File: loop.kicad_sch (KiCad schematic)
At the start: 0 parts

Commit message: schematic
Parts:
- added BT1: Battery_Cell, Package_DFN_QFN:QFN-40-1EP_6x6mm_P0.5mm_EP4.6x4.6mm, symbol Device:Battery_Cell
- added D1: LED, symbol Device:LED
- added SW1: SW_SPST, symbol Switch:SW_SPST
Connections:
- new net: BT1.2 (-), D1.1 (K)
- new net: D1.2 (A), SW1.2 (B)
- new net: BT1.1 (+), SW1.1 (A)

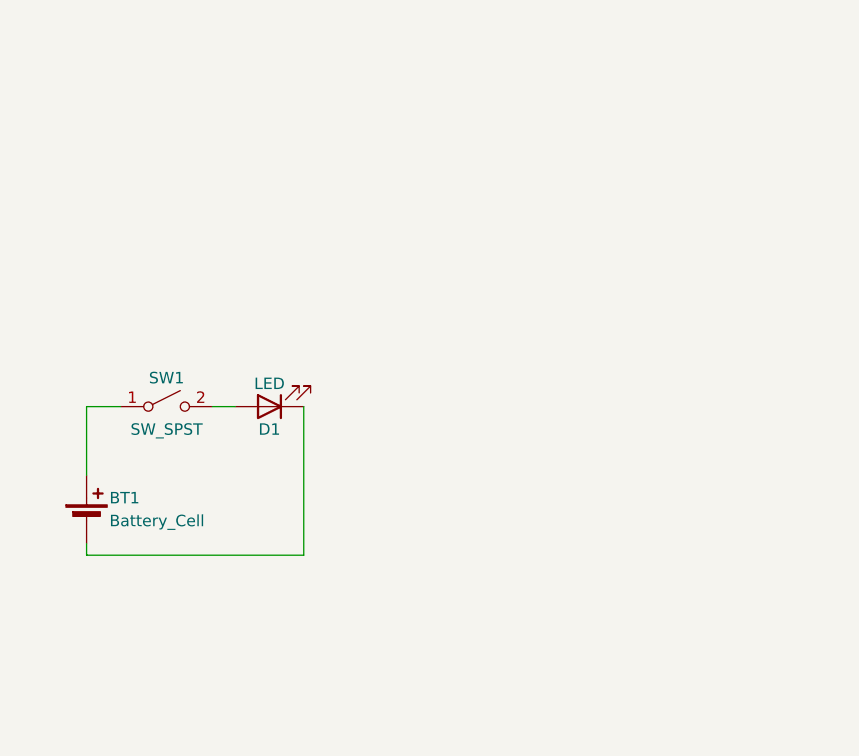
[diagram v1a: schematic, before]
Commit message: build latch schematic using dual flip flop
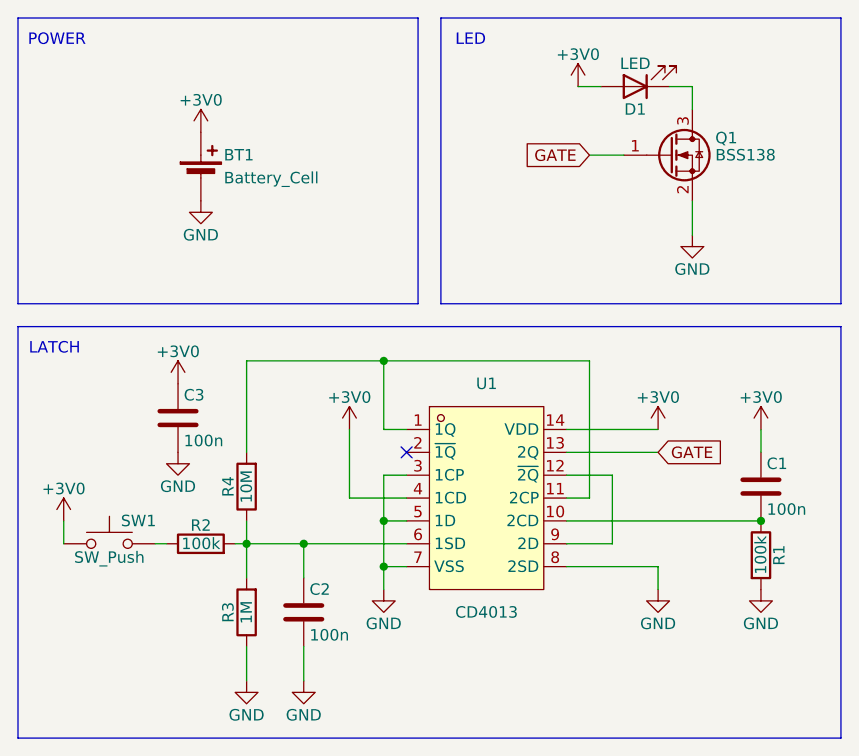
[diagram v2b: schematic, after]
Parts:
- removed SW1: SW_SPST, symbol Switch:SW_SPST
- added C1, C2, C3: 100n, Package_TO_SOT_SMD:SOT-23, symbol Device:C
- added Q1: BSS138, Package_TO_SOT_SMD:SOT-23, symbol Transistor_FET:BSS138
- added R1, R2: 100k, symbol Device:R
- added R3: 1M, symbol Device:R
- added R4: 10M, symbol Device:R
- added SW1: SW_Push, SparkFun-Switch:Push_PTH_12x12mm, symbol Switch:SW_Push
- added U1: CD4013, easyeda2kicad:SOP-14_L8.7-W3.9-P1.27-LS6.0-BL, symbol LCSC:CD4013
- BT1: footprint Package_DFN_QFN:QFN-40-1EP_6x6mm_P0.5mm_EP4.6x4.6mm -> Battery:BatteryHolder_Multicomp_BC-2001_1x2032
- D1: footprint (none) -> 0_CustomFootprints:Led Nood
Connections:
- net at D1.1 (K): now also Q1.3 (D); no longer BT1.2 (-)
- net +3V0: now reaches D1.2 (A)
- net +3V0: now also BT1.1 (+), C1.1, C3.1, SW1.1, U1.14 (VDD), U1.4 (1CD)
- new net: C2.1, R2.2, R3.2, R4.1, U1.6 (1SD)
- new net: R4.2, U1.1 (1Q), U1.11 (2CP)
- new net: C1.2, R1.1, U1.10 (2CD)
- new net: U1.12 (~{2Q}), U1.9 (2D)
- new net: R2.1, SW1.2
- new net GATE: Q1.1 (G), U1.13 (2Q)
- new net GND: BT1.2 (-), C2.2, C3.2, Q1.2 (S), R1.2, R3.1, U1.3 (1CP), U1.5 (1D), U1.7 (VSS), U1.8 (2SD)
- no-connect marks 0 -> 1
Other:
- note added: "LATCH"
- note added: "LED"
- note added: "POWER"
- company: (none) -> Paul Methfessel
- title: (none) -> Loop
- moved on the sheet: BT1, D1

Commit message: build pcb layout
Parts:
- C1, C2, C3: footprint Package_TO_SOT_SMD:SOT-23 -> Capacitor_SMD:C_0805_2012Metric_Pad1.18x1.45mm_HandSolder
- R1, R2, R3, R4: footprint (none) -> Resistor_SMD:R_0805_2012Metric_Pad1.20x1.40mm_HandSolder
- SW1: footprint SparkFun-Switch:Push_PTH_12x12mm -> Button_Switch_SMD:SW_SPST_TL3342
- U1: footprint easyeda2kicad:SOP-14_L8.7-W3.9-P1.27-LS6.0-BL -> LCSC:SOP-14_L8.7-W3.9-P1.27-LS6.0-BL
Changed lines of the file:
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@@
 			)
 		)
-		(property "Footprint" "Package_TO_SOT_SMD:SOT-23"
+		(property "Footprint" "Capacitor_SMD:C_0805_2012Metric_Pad1.18x1.45mm_HandSolder"
 			(at 116.5352 92.71 0)
 			(hide yes)
@@
 			)
 		)
-		(property "Footprint" ""
+		(property "Footprint" "Resistor_SMD:R_0805_2012Metric_Pad1.20x1.40mm_HandSolder"
 			(at 124.968 96.52 90)
 			(hide yes)
@@
 			)
 		)
-		(property "Footprint" ""
+		(property "Footprint" "Resistor_SMD:R_0805_2012Metric_Pad1.20x1.40mm_HandSolder"
 			(at 178.562 104.14 90)
 			(hide yes)
@@
 			)
 		)
-		(property "Footprint" "easyeda2kicad:SOP-14_L8.7-W3.9-P1.27-LS6.0-BL"
+		(property "Footprint" "LCSC:SOP-14_L8.7-W3.9-P1.27-LS6.0-BL"
 			(at 149.86 113.03 0)
 			(hide yes)
@@
 			)
 		)
-		(property "Footprint" "Package_TO_SOT_SMD:SOT-23"
+		(property "Footprint" "Capacitor_SMD:C_0805_2012Metric_Pad1.18x1.45mm_HandSolder"
 			(at 181.3052 100.33 0)
 			(hide yes)
@@
 			)
 		)
-		(property "Footprint" ""
+		(property "Footprint" "Resistor_SMD:R_0805_2012Metric_Pad1.20x1.40mm_HandSolder"
 			(at 124.968 110.49 90)
 			(hide yes)
@@
 			)
 		)
-		(property "Footprint" ""
+		(property "Footprint" "Resistor_SMD:R_0805_2012Metric_Pad1.20x1.40mm_HandSolder"
 			(at 118.11 104.648 90)
 			(hide yes)
@@
 			)
 		)
-		(property "Footprint" "Package_TO_SOT_SMD:SOT-23"
+		(property "Footprint" "Capacitor_SMD:C_0805_2012Metric_Pad1.18x1.45mm_HandSolder"
 			(at 130.5052 114.3 0)
 			(hide yes)
@@
 			)
 		)
-		(property "Footprint" "SparkFun-Switch:Push_PTH_12x12mm"
+		(property "Footprint" "Button_Switch_SMD:SW_SPST_TL3342"
 			(at 107.95 97.79 0)
 			(hide yes)

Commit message: Add series r
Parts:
- removed C3: 100n, Capacitor_SMD:C_0805_2012Metric_Pad1.18x1.45mm_HandSolder, symbol Device:C
- added C4: 22u, Capacitor_SMD:C_0805_2012Metric_Pad1.18x1.45mm_HandSolder, symbol Device:C
- added C5: 10u, Capacitor_SMD:C_0805_2012Metric_Pad1.18x1.45mm_HandSolder, symbol Device:C
- added R5: 1k, Resistor_SMD:R_0805_2012Metric_Pad1.20x1.40mm_HandSolder, symbol Device:R
- added R6: 33, Resistor_SMD:R_0805_2012Metric_Pad1.20x1.40mm_HandSolder, symbol Device:R
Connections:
- net +3V0: now also C4.1, R5.1, R6.1; no longer D1.2 (A), U1.14 (VDD), U1.4 (1CD)
- net GND: now also C4.2, C5.2
- new net: D1.2 (A), R6.2
- new net V_F: C5.1, R5.2, U1.14 (VDD), U1.4 (1CD)
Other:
- moved on the sheet: BT1, C1, D1, Q1, R1

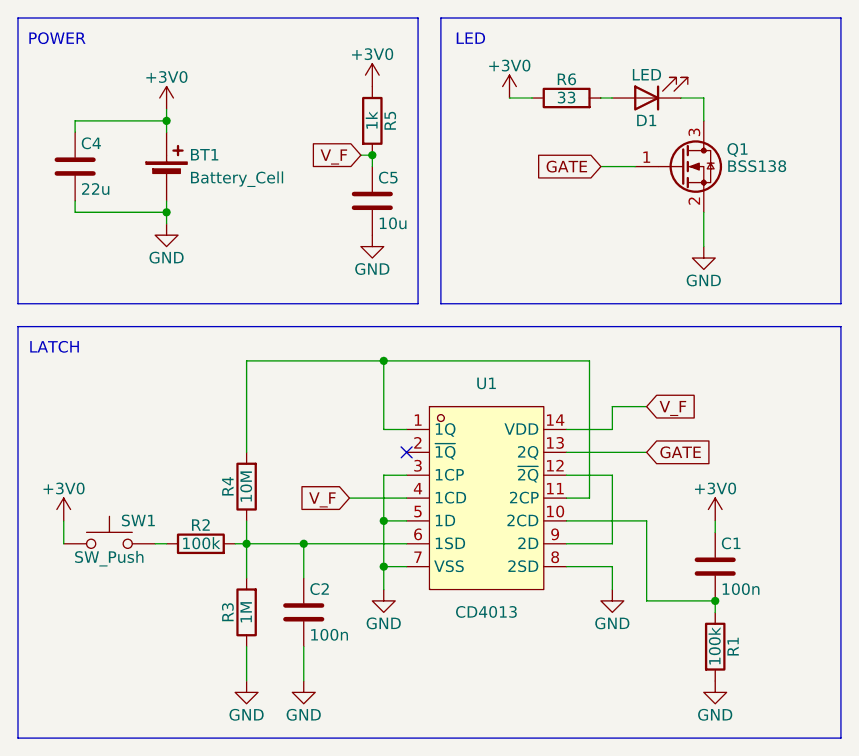
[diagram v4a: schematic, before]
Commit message: Use Attiny202
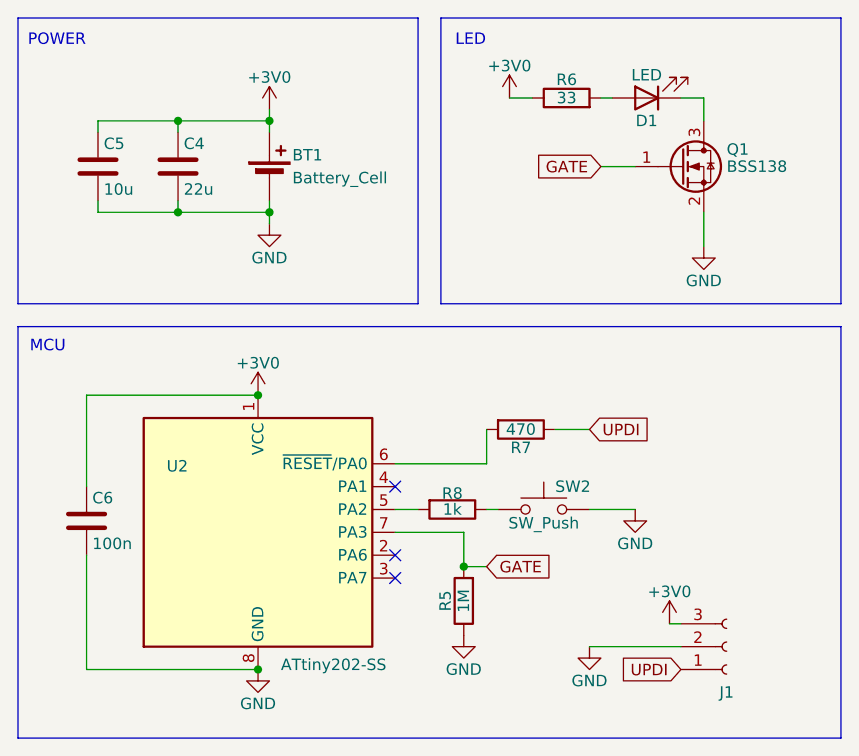
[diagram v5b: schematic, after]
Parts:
- removed C1, C2: 100n, Capacitor_SMD:C_0805_2012Metric_Pad1.18x1.45mm_HandSolder, symbol Device:C
- removed R1, R2: 100k, Resistor_SMD:R_0805_2012Metric_Pad1.20x1.40mm_HandSolder, symbol Device:R
- removed R3: 1M, Resistor_SMD:R_0805_2012Metric_Pad1.20x1.40mm_HandSolder, symbol Device:R
- removed R4: 10M, Resistor_SMD:R_0805_2012Metric_Pad1.20x1.40mm_HandSolder, symbol Device:R
- removed SW1: SW_Push, Button_Switch_SMD:SW_SPST_TL3342, symbol Switch:SW_Push
- removed U1: CD4013, LCSC:SOP-14_L8.7-W3.9-P1.27-LS6.0-BL, symbol LCSC:CD4013
- added C6: 100n, Capacitor_SMD:C_0805_2012Metric_Pad1.18x1.45mm_HandSolder, symbol Device:C
- added J1: Conn_01x03_Socket, Connector:Tag-Connect_TC2030-IDC-FP_2x03_P1.27mm_Vertical, symbol Connector:Conn_01x03_Socket
- added R7: 470, Resistor_SMD:R_0805_2012Metric_Pad1.20x1.40mm_HandSolder, symbol Device:R
- added R8: 1k, Resistor_SMD:R_0805_2012Metric_Pad1.20x1.40mm_HandSolder, symbol Device:R
- added SW2: SW_Push, Button_Switch_SMD:SW_SPST_TL3342, symbol Switch:SW_Push
- added U2: ATtiny202-SS, Package_SO:SOIC-8_3.9x4.9mm_P1.27mm, symbol MCU_Microchip_ATtiny:ATtiny202-SS
- R5: value 1k -> 1M
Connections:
- net +3V0: now also C5.1, C6.1, J1.3 (Pin_3), U2.1 (VCC); no longer R5.1
- net GATE: now also R5.2, U2.7 (PA3)
- net GND: now also R5.1, C6.2, J1.2 (Pin_2), SW2.2, U2.8 (GND)
- removed net V_F: C5.1, R5.2
- new net: R8.1, SW2.1
- new net: R8.2, U2.5 (PA2)
- new net: R7.2, U2.6 (~{RESET}/PA0)
- new net UPDI: J1.1 (Pin_1), R7.1
- no-connect marks 1 -> 3
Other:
- note added: "MCU"
- note removed: "LATCH"
- moved on the sheet: BT1, C4

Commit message: Update PCB
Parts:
- BT1: footprint Battery:BatteryHolder_Multicomp_BC-2001_1x2032 -> easyeda2kicad:BAT-SMD_MY-1220-03
- J1: footprint Connector:Tag-Connect_TC2030-IDC-FP_2x03_P1.27mm_Vertical -> Connector_PinSocket_2.54mm:PinSocket_1x03_P2.54mm_Vertical
- renumbered C6 to C1, C5 to C2, C4 to C3, R8 to R1, R5 to R2, R7 to R3, R6 to R4, SW2 to SW1, U2 to U1
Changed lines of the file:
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@@
 		(in_pos_files yes)
 		(dnp no)
-		(property "Reference" "C4"
+		(property "Reference" "C3"
 			(at 116.205 58.42 0)
 			(show_name no)
@@
 			(project "loop"
 				(path "/b044b678-0750-420d-a2ee-3e7506caa1d8"
-					(reference "C4")
+					(reference "C3")
 					(unit 1)
 				)
@@
 		(in_pos_files yes)
 		(dnp no)
-		(property "Reference" "C6"
+		(property "Reference" "C1"
 			(at 106.045 97.79 0)
 			(show_name no)
@@
 			(project "loop"
 				(path "/b044b678-0750-420d-a2ee-3e7506caa1d8"
-					(reference "C6")
+					(reference "C1")
 					(unit 1)
 				)
@@
 		(in_pos_files yes)
 		(dnp no)
-		(property "Reference" "#PWR04"
+		(property "Reference" "#PWR09"
 			(at 170.18 115.57 0)
 			(hide yes)
@@
 			(project "loop"
 				(path "/b044b678-0750-420d-a2ee-3e7506caa1d8"
-					(reference "#PWR04")
+					(reference "#PWR09")
 					(unit 1)
 				)
@@
 		(in_pos_files yes)
 		(dnp no)
-		(property "Reference" "R5"
+		(property "Reference" "R2"
 			(at 145.288 109.22 90)
 			(show_name no)
@@
 			(project "loop"
 				(path "/b044b678-0750-420d-a2ee-3e7506caa1d8"
-					(reference "R5")
+					(reference "R2")
 					(unit 1)
 				)
@@
 		(in_pos_files yes)
 		(dnp no)
-		(property "Reference" "#PWR08"
+		(property "Reference" "#PWR010"
 			(at 173.99 76.2 0)
 			(hide yes)
@@
 			(project "loop"
 				(path "/b044b678-0750-420d-a2ee-3e7506caa1d8"
-					(reference "#PWR08")
+					(reference "#PWR010")
 					(unit 1)
 				)
@@
 		(in_pos_files yes)
 		(dnp no)
-		(property "Reference" "#PWR015"
+		(property "Reference" "#PWR05"
 			(at 147.32 119.38 0)
 			(hide yes)
@@
 			(project "loop"
 				(path "/b044b678-0750-420d-a2ee-3e7506caa1d8"
-					(reference "#PWR015")
+					(reference "#PWR05")
 					(unit 1)
 				)
@@
 		(in_pos_files yes)
 		(dnp no)
-		(property "Reference" "R8"
+		(property "Reference" "R1"
 			(at 146.05 97.282 90)
 			(show_name no)
@@
 			(project "loop"
 				(path "/b044b678-0750-420d-a2ee-3e7506caa1d8"
-					(reference "R8")
+					(reference "R1")
 					(unit 1)
 				)
@@
 		(in_pos_files yes)
 		(dnp no)
-		(property "Reference" "C5"
+		(property "Reference" "C2"
 			(at 107.315 58.42 0)
 			(show_name no)
@@
 			(project "loop"
 				(path "/b044b678-0750-420d-a2ee-3e7506caa1d8"
-					(reference "C5")
+					(reference "C2")
 					(unit 1)
 				)
@@
 			)
 		)
-		(property "Footprint" "Connector:Tag-Connect_TC2030-IDC-FP_2x03_P1.27mm_Vertical"
+		(property "Footprint" "Connector_PinSocket_2.54mm:PinSocket_1x03_P2.54mm_Vertical"
 			(at 176.53 114.3 0)
 			(hide yes)
@@
 		(in_pos_files yes)
 		(dnp no)
-		(property "Reference" "SW2"
+		(property "Reference" "SW1"
 			(at 157.48 96.52 0)
 			(show_name no)
@@
 			(project "loop"
 				(path "/b044b678-0750-420d-a2ee-3e7506caa1d8"
-					(reference "SW2")
+					(reference "SW1")
 					(unit 1)
 				)
@@
 		(in_pos_files yes)
 		(dnp no)
-		(property "Reference" "#PWR017"
+		(property "Reference" "#PWR07"
 			(at 161.29 120.65 0)
 			(hide yes)
@@
 			(project "loop"
 				(path "/b044b678-0750-420d-a2ee-3e7506caa1d8"
-					(reference "#PWR017")
+					(reference "#PWR07")
 					(unit 1)
 				)
@@
 		(in_pos_files yes)
 		(dnp no)
-		(property "Reference" "#PWR07"
+		(property "Reference" "#PWR06"
 			(at 152.4 57.15 0)
 			(hide yes)
@@
 			(project "loop"
 				(path "/b044b678-0750-420d-a2ee-3e7506caa1d8"
-					(reference "#PWR07")
+					(reference "#PWR06")
 					(unit 1)
 				)
@@
 		(in_pos_files yes)
 		(dnp no)
-		(property "Reference" "R7"
+		(property "Reference" "R3"
 			(at 153.67 92.202 90)
 			(show_name no)
@@
 			(project "loop"
 				(path "/b044b678-0750-420d-a2ee-3e7506caa1d8"
-					(reference "R7")
+					(reference "R3")
 					(unit 1)
 				)
@@
 		(in_pos_files yes)
 		(dnp no)
-		(property "Reference" "#PWR03"
+		(property "Reference" "#PWR01"
 			(at 124.46 90.17 0)
 			(hide yes)
@@
 			(project "loop"
 				(path "/b044b678-0750-420d-a2ee-3e7506caa1d8"
-					(reference "#PWR03")
+					(reference "#PWR01")
 					(unit 1)
 				)
@@
 		(in_pos_files yes)
 		(dnp no)
-		(property "Reference" "#PWR02"
+		(property "Reference" "#PWR04"
 			(at 125.73 73.66 0)
 			(hide yes)
@@
 			(project "loop"
 				(path "/b044b678-0750-420d-a2ee-3e7506caa1d8"
-					(reference "#PWR02")
+					(reference "#PWR04")
 					(unit 1)
 				)
@@
 		(in_pos_files yes)
 		(dnp no)
-		(property "Reference" "#PWR016"
+		(property "Reference" "#PWR08"
 			(at 166.37 105.41 0)
 			(hide yes)
@@
 			(project "loop"
 				(path "/b044b678-0750-420d-a2ee-3e7506caa1d8"
-					(reference "#PWR016")
+					(reference "#PWR08")
 					(unit 1)
 				)
@@
 		(in_pos_files yes)
 		(dnp no)
-		(property "Reference" "R6"
+		(property "Reference" "R4"
 			(at 158.75 51.308 90)
 			(show_name no)
@@
 			(project "loop"
 				(path "/b044b678-0750-420d-a2ee-3e7506caa1d8"
-					(reference "R6")
+					(reference "R4")
 					(unit 1)
 				)
@@
 		(in_pos_files yes)
 		(dnp no)
-		(property "Reference" "U2"
+		(property "Reference" "U1"
 			(at 114.3 94.996 0)
 			(show_name no)
@@
 			(project "loop"
 				(path "/b044b678-0750-420d-a2ee-3e7506caa1d8"
-					(reference "U2")
+					(reference "U1")
 					(unit 1)
 				)
@@
 			)
 		)
-		(property "Footprint" "Battery:BatteryHolder_Multicomp_BC-2001_1x2032"
+		(property "Footprint" "easyeda2kicad:BAT-SMD_MY-1220-03"
 			(at 125.73 60.706 90)
 			(hide yes)
@@
 		(in_pos_files yes)
 		(dnp no)
-		(property "Reference" "#PWR01"
+		(property "Reference" "#PWR03"
 			(at 125.73 58.42 0)
 			(hide yes)
@@
 			(project "loop"
 				(path "/b044b678-0750-420d-a2ee-3e7506caa1d8"
-					(reference "#PWR01")
+					(reference "#PWR03")
 					(unit 1)
 				)
@@
 		(in_pos_files yes)
 		(dnp no)
-		(property "Reference" "#PWR014"
+		(property "Reference" "#PWR02"
 			(at 124.46 123.19 0)
 			(hide yes)
@@
 			(project "loop"
 				(path "/b044b678-0750-420d-a2ee-3e7506caa1d8"
-					(reference "#PWR014")
-					(unit 1)
-				)
+					(reference "#PWR02")
+					(unit 1)
+				)
